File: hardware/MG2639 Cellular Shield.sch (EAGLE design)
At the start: 50 parts, among them J1 SIMHOLDER, Q1 MMBT2222A, Q2 MMBT2222A, U1 TXB0108, U2 SPX29302, U4 ARDUINO_R3_SHIELDNOLABELS, U5 MG2639V3

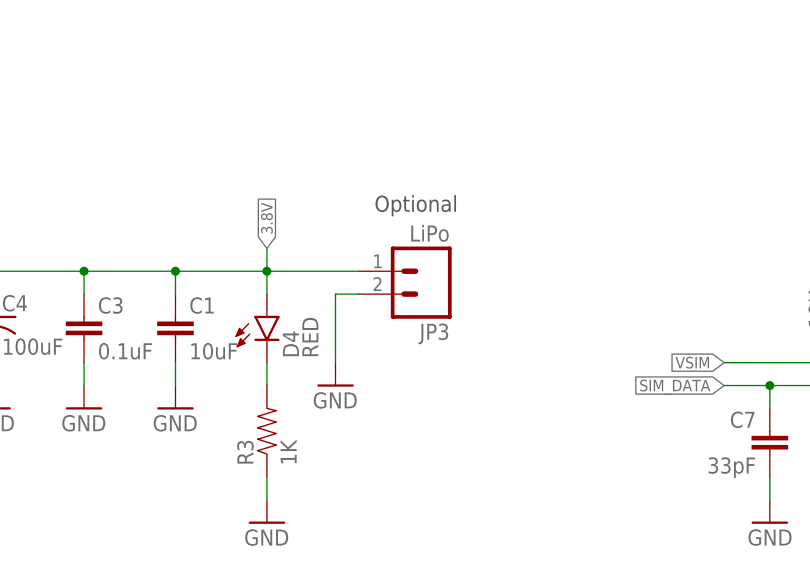
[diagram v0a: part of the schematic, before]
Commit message: Corrected +/- on battery connector
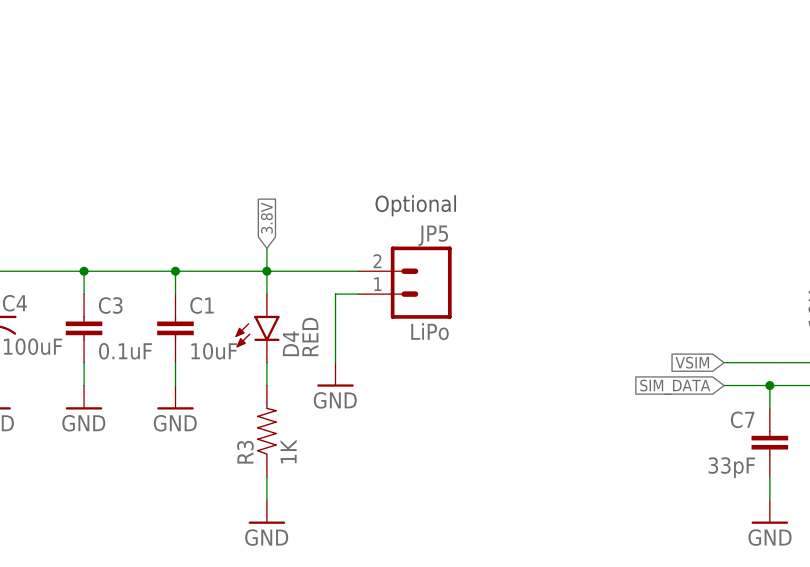
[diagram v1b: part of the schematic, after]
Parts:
- removed JP3: LiPo, SparkFun-Connectors:M02JST-PTH-2
- added JP5: LiPo, SparkFun-Connectors:M02JST-PTH-2
- C10, C11, C3: device SparkFun:CAP0603-CAP -> SparkFun-Capacitors:0.1UF-25V(+80/-20%)(0603)
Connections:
- net 3.8V: now also JP5.2; no longer JP3.1
- net GND: now also JP5.1; no longer JP3.2

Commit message: Prelim firmware. Works for certain features.
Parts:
- BAT1: value 20mm coincell -> 12mm coincell
- D2: value RED -> BLUE; device SparkFun-LED:LED-RED1206 -> SparkFun-LED:LED-BLUE1206
- U4: value ARDUINO_R3_SHIELDNOLABELS -> ARDUINO_R3_SHIELD
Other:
- note added: "N. Seidle"
- note added: "Open SJ1 to disconnect GPS power from board power."
- note added: "Open SJ2 to free up GPIO and power up via boot button."
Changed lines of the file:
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@@
 <part name="GND12" library="SparkFun" deviceset="GND" device=""/>
 <part name="C4" library="SparkFun-Capacitors" deviceset="100UF-10V-10%(TANT)" device="" value="100uF"/>
-<part name="U4" library="SparkFun-Boards" deviceset="ARDUINO_R3_SHIELD" device="NOLABELS" value="ARDUINO_R3_SHIELDNOLABELS"/>
+<part name="U4" library="SparkFun-Boards" deviceset="ARDUINO_R3_SHIELD" device="NOLABELS" value="ARDUINO_R3_SHIELD"/>
 <part name="Q1" library="SparkFun-DiscreteSemi" deviceset="TRANSISTOR_NPN" device="MMBT2222A" value="MMBT2222A"/>
 <part name="Q2" library="SparkFun-DiscreteSemi" deviceset="TRANSISTOR_NPN" device="MMBT2222A" value="MMBT2222A"/>
@@
 <part name="GND13" library="SparkFun" deviceset="GND" device=""/>
 <part name="SJ1" library="SparkFun-Passives" deviceset="JUMPER-PAD-2-NC_BY_TRACE" device="" value=""/>
-<part name="BAT1" library="SparkFun-Electromechanical" deviceset="BATTERY" device="12MM" value="20mm coincell"/>
+<part name="BAT1" library="SparkFun-Electromechanical" deviceset="BATTERY" device="12MM" value="12mm coincell"/>
 <part name="GND15" library="SparkFun" deviceset="GND" device=""/>
 <part name="GND16" library="SparkFun" deviceset="GND" device=""/>
@@
 <part name="R8" library="SparkFun-Resistors" deviceset="1KOHM1/10W1%(0603)" device="" value="1K"/>
 <part name="GND18" library="SparkFun" deviceset="GND" device=""/>
-<part name="D2" library="SparkFun-LED" deviceset="LED-RED" device="1206" value="RED"/>
+<part name="D2" library="SparkFun-LED" deviceset="LED-BLUE" device="1206" value="BLUE"/>
 <part name="R9" library="SparkFun-Resistors" deviceset="1KOHM1/10W1%(0603)" device="" value="1K"/>
 <part name="GND19" library="SparkFun" deviceset="GND" device=""/>
@@
 for antenna U.FL
 wire relief</text>
+<text x="20.32" y="2.54" size="1.778" layer="97">N. Seidle</text>
+<text x="7.62" y="170.18" size="1.778" layer="97">Open SJ1 to disconnect GPS
+power from board power.</text>
+<text x="88.9" y="149.86" size="1.778" layer="97">Open SJ2 to free up GPIO
+and power up via boot button.</text>
 </plain>
 <instances>
@@
 <attribute name="VALUE" x="22.86" y="152.4" size="1.778" layer="96"/>
 </instance>
-<instance part="BAT1" gate="G$1" x="109.22" y="109.22" rot="R270"/>
+<instance part="BAT1" gate="G$1" x="109.22" y="109.22" smashed="yes" rot="R270">
+<attribute name="NAME" x="116.332" y="105.41" size="1.778" layer="95" rot="R90"/>
+<attribute name="VALUE" x="103.632" y="100.076" size="1.778" layer="96" rot="R90"/>
+</instance>
 <instance part="GND15" gate="1" x="109.22" y="99.06" rot="MR0"/>
 <instance part="GND16" gate="1" x="30.48" y="38.1" rot="MR0"/>

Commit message: Add silk labels to pins/jumpers. Add FTDI header. Remove SYSRST circuit. Reconfiguring jumpers. Removed USB connector, broke USB pins out to headers.
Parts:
- removed LOGO1: SFE_LOGO_NAME_FLAME.1_INCH, SparkFun-Aesthetics:SFE_LOGO_NAME_FLAME.1_INCH
- removed Q2: MMBT2222A, SparkFun-DiscreteSemi:TRANSISTOR_NPNMMBT2222A
- removed R11, R12: 22, SparkFun-Resistors:22OHM1/10W1%(0603)
- removed R13: 4.7K, SparkFun-Resistors:4.7KOHM1/10W1%(0603)
- removed U$1: CREATIVE_COMMONS, SparkFun:CREATIVE_COMMONS
- removed U$2: SMA_HOLE, SparkFun-RF:SMA_HOLE
- added FRAME1: FRAME-LEDGER, SparkFun-Aesthetics:FRAME-LEDGER
- added JP3: M01PTH, SparkFun-Connectors:M01PTH
- added JP6: FTDI_BASICPTH, SparkFun-Connectors:FTDI_BASICPTH
- added LOGO4: SFE_LOGO_NAME.1_INCH, SparkFun-Aesthetics:SFE_LOGO_NAME.1_INCH
- added R5: 1K, SparkFun-Resistors:1KOHM1/10W1%(0603)
- JP1: value USBSMD -> (none); device SparkFun-Connectors:USBSMD -> SparkFun-Connectors:M05PTH
- JP2: value (none) -> AUDIO
- S2: value BOOT -> RESET
- SJ2: value JUMPER-PAD-2-NC_BY_TRACE -> JUMPER-PAD-3-2OF3_NC_BY_TRACE; device SparkFun-Passives:JUMPER-PAD-2-NC_BY_TRACE -> SparkFun-Passives:JUMPER-PAD-3-2OF3_NC_BY_TRACE
- SJ3, SJ4, SJ5: value JUMPER-PAD-3-2OF3_NC_BY_PASTE -> JUMPER-PAD-3-2OF3_NC_BY_TRACE; device SparkFun-Passives:JUMPER-PAD-3-2OF3_NC_BY_PASTE -> SparkFun-Passives:JUMPER-PAD-3-2OF3_NC_BY_TRACE
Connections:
- removed net N$10: JP1.D+, R11.1
- removed net N$11: JP1.D-, R12.1
- removed net N$2: Q2.B, R13.2
- new net N$6: R5.1, SJ2.1
- net !SYSRST: now also JP3.1; no longer Q2.C
- net 5V: now also R5.2
- net CELL_RESET: no longer R13.1
- net GND: now also JP1.1, JP6.6; no longer JP1.GND, Q2.E
- net GRX-HV: now also JP6.3
- net GTX-HV: now also JP6.2
- net ON/OFF: now also SJ2.3; no longer SJ2.1
- net RX-SOFT: now also SJ4.3; no longer SJ4.1
- net RXI: now also SJ4.1; no longer SJ4.3
- net TX-SOFT: now also SJ3.3; no longer SJ3.1
- net TXO: now also SJ3.1; no longer SJ3.3
- net USB+: now also JP1.3; no longer R11.2
- net USB-: now also JP1.4; no longer R12.2
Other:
- note added: "Arduino Shield"
- note added: "Boot Button"
- note added: "GPS Battery"
- note added: "Level Shifter"
- note added: "MG2639 Cellular Module"
- note added: "Misc. Headers"
- note added: "Nathan Seidle Jim Lindblom"
- note added: "SIM Card"
- note added: "Select between hardware UART and software UART Default = Software"
- note added: "UART Select"
- note added: "Voltage Regulator"
- note added: "v10"
- note removed: "GRX-2.8V"
- note removed: "GTX"
- note removed: "Holes in board are for antenna U.FL wire relief"
- note removed: "N. Seidle"
- note removed: "Open SJ2 to free up GPIO and power up via boot button."
- note removed: "SMA Bulkhead mount Experimental"
- note removed: "Select between hardware UART and software UART Default = Hardware"
- note removed: "TX-2.8V"
- note removed: "TX-HV"
- note removed: "USB Port Experimental"
- moved on the sheet: BAT1, C1, C10, C11, C2, C3, C4, C5, C6, C7, C8, C9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

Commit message: re-routing around TXB0108, cleaning up some silk.
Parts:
- added FID1, FID2: FIDUCIAL1X2, SparkFun-Aesthetics:FIDUCIAL1X2
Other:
- moved on the sheet: S2

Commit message: adding 22 ohm resistors to D+/D-. placing more vias around vreg.
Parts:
- added R11, R7: 22, SparkFun-Resistors:22OHM1/10W1%(0603)
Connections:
- new net N$10: JP1.3, R11.1
- new net N$2: JP1.4, R7.1
- net USB+: now also R11.2; no longer JP1.3
- net USB-: now also R7.2; no longer JP1.4
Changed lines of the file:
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@@
 <part name="SUPPLY4" library="SparkFun-Aesthetics" deviceset="5V" device=""/>
 <part name="SUPPLY5" library="SparkFun-Aesthetics" deviceset="3.3V" device=""/>
+<part name="R7" library="SparkFun-Resistors" deviceset="22OHM1/10W1%(0603)" device="" value="22"/>
+<part name="R11" library="SparkFun-Resistors" deviceset="22OHM1/10W1%(0603)" device="" value="22"/>
 </parts>
 <sheets>
@@
 <instance part="SUPPLY4" gate="G$1" x="388.62" y="233.68"/>
 <instance part="SUPPLY5" gate="G$1" x="393.7" y="233.68"/>
+<instance part="R7" gate="G$1" x="358.14" y="119.38" smashed="yes">
+<attribute name="NAME" x="359.8164" y="120.5992" size="1.778" layer="95"/>
+<attribute name="VALUE" x="354.7364" y="120.5992" size="1.778" layer="96"/>
+</instance>
+<instance part="R11" gate="G$1" x="358.14" y="116.84" smashed="yes">
+<attribute name="NAME" x="358.902" y="113.7666" size="1.778" layer="95"/>
+<attribute name="VALUE" x="353.822" y="113.7666" size="1.778" layer="96"/>
+</instance>
 </instances>
 <busses>
@@
 <net name="USB+" class="0">
 <segment>
-<label x="355.6" y="116.84" size="1.27" layer="95" xref="yes"/>
-<wire x1="347.98" y1="116.84" x2="355.6" y2="116.84" width="0.1524" layer="91"/>
-<pinref part="JP1" gate="G$1" pin="3"/>
-</segment>
-<segment>
 <pinref part="U5" gate="U1" pin="USB_DP"/>
 <wire x1="241.3" y1="68.58" x2="243.84" y2="68.58" width="0.1524" layer="91"/>
 <label x="243.84" y="68.58" size="1.27" layer="95" xref="yes"/>
 </segment>
+<segment>
+<pinref part="R11" gate="G$1" pin="2"/>
+<wire x1="363.22" y1="116.84" x2="365.76" y2="116.84" width="0.1524" layer="91"/>
+<label x="365.76" y="116.84" size="1.27" layer="95" xref="yes"/>
+</segment>
 </net>
 <net name="USB-" class="0">
-<segment>
-<label x="355.6" y="119.38" size="1.27" layer="95" xref="yes"/>
-<wire x1="347.98" y1="119.38" x2="355.6" y2="119.38" width="0.1524" layer="91"/>
-<pinref part="JP1" gate="G$1" pin="4"/>
-</segment>
 <segment>
 <pinref part="U5" gate="U1" pin="USB_DM"/>
 <wire x1="241.3" y1="66.04" x2="243.84" y2="66.04" width="0.1524" layer="91"/>
 <label x="243.84" y="66.04" size="1.27" layer="95" xref="yes"/>
+</segment>
+<segment>
+<pinref part="R7" gate="G$1" pin="2"/>
+<wire x1="363.22" y1="119.38" x2="365.76" y2="119.38" width="0.1524" layer="91"/>
+<label x="365.76" y="119.38" size="1.27" layer="95" xref="yes"/>
 </segment>
 </net>
@@
 </segment>
 </net>
+<net name="N$2" class="0">
+<segment>
+<pinref part="R7" gate="G$1" pin="1"/>
+<pinref part="JP1" gate="G$1" pin="4"/>
+<wire x1="353.06" y1="119.38" x2="347.98" y2="119.38" width="0.1524" layer="91"/>
+</segment>
+</net>
+<net name="N$10" class="0">
+<segment>
+<pinref part="R11" gate="G$1" pin="1"/>
+<pinref part="JP1" gate="G$1" pin="3"/>
+<wire x1="353.06" y1="116.84" x2="347.98" y2="116.84" width="0.1524" layer="91"/>
+</segment>
+</net>

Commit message: rearranging LEDs - moving GPS LED up with others.
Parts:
- added JP7: M01PTH, SparkFun-Connectors:M01PTH
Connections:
- new net ADCIN: U5.ADCIN
- new net GPIO0: U5.GPIO0/PWM
- new net GPIO1: U5.GPIO1/SCL
- new net GPIO2: U5.GPIO2/SDA
- net VDDIO: now also JP7.1
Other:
- moved on the sheet: JP2
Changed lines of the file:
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@@
 <part name="R7" library="SparkFun-Resistors" deviceset="22OHM1/10W1%(0603)" device="" value="22"/>
 <part name="R11" library="SparkFun-Resistors" deviceset="22OHM1/10W1%(0603)" device="" value="22"/>
+<part name="JP7" library="SparkFun-Connectors" deviceset="M01" device="PTH" value="M01PTH"/>
 </parts>
 <sheets>
@@
 <instance part="JP4" gate="G$1" x="340.36" y="144.78" rot="MR180"/>
 <instance part="GND27" gate="1" x="350.52" y="137.16"/>
-<instance part="JP2" gate="G$1" x="259.08" y="55.88" rot="R180"/>
-<instance part="GND3" gate="1" x="251.46" y="40.64" rot="MR0"/>
+<instance part="JP2" gate="G$1" x="264.16" y="55.88" rot="R180"/>
+<instance part="GND3" gate="1" x="256.54" y="40.64" rot="MR0"/>
 <instance part="C10" gate="G$1" x="210.82" y="251.46"/>
 <instance part="C11" gate="G$1" x="223.52" y="251.46"/>
@@
 <attribute name="VALUE" x="353.822" y="113.7666" size="1.778" layer="96"/>
 </instance>
+<instance part="JP7" gate="G$1" x="337.82" y="165.1"/>
 </instances>
 <busses>
@@
 <segment>
 <pinref part="JP2" gate="G$1" pin="7"/>
-<wire x1="254" y1="45.72" x2="251.46" y2="45.72" width="0.1524" layer="91"/>
-<wire x1="251.46" y1="45.72" x2="251.46" y2="43.18" width="0.1524" layer="91"/>
+<wire x1="259.08" y1="45.72" x2="256.54" y2="45.72" width="0.1524" layer="91"/>
+<wire x1="256.54" y1="45.72" x2="256.54" y2="43.18" width="0.1524" layer="91"/>
 <pinref part="GND3" gate="1" pin="GND"/>
 </segment>
@@
 <label x="210.82" y="259.08" size="1.27" layer="95" rot="R90" xref="yes"/>
 </segment>
+<segment>
+<pinref part="JP7" gate="G$1" pin="1"/>
+<wire x1="345.44" y1="165.1" x2="347.98" y2="165.1" width="0.1524" layer="91"/>
+<label x="347.98" y="165.1" size="1.27" layer="95" xref="yes"/>
+</segment>
 </net>
 <net name="USB+" class="0">
@@
 <segment>
 <pinref part="U5" gate="U1" pin="MIC_P1"/>
-<wire x1="241.3" y1="55.88" x2="254" y2="55.88" width="0.1524" layer="91"/>
+<wire x1="241.3" y1="55.88" x2="259.08" y2="55.88" width="0.1524" layer="91"/>
 <pinref part="JP2" gate="G$1" pin="3"/>
 </segment>
@@
 <segment>
 <pinref part="U5" gate="U1" pin="MIC_P0"/>
-<wire x1="241.3" y1="58.42" x2="254" y2="58.42" width="0.1524" layer="91"/>
+<wire x1="241.3" y1="58.42" x2="259.08" y2="58.42" width="0.1524" layer="91"/>
 <pinref part="JP2" gate="G$1" pin="2"/>
 </segment>
@@
 <segment>
 <pinref part="U5" gate="U1" pin="MIC_N0"/>
-<wire x1="241.3" y1="60.96" x2="254" y2="60.96" width="0.1524" layer="91"/>
+<wire x1="241.3" y1="60.96" x2="259.08" y2="60.96" width="0.1524" layer="91"/>
 <pinref part="JP2" gate="G$1" pin="1"/>
 </segment>
@@
 <segment>
 <pinref part="U5" gate="U1" pin="RECN"/>
-<wire x1="241.3" y1="53.34" x2="254" y2="53.34" width="0.1524" layer="91"/>
+<wire x1="241.3" y1="53.34" x2="259.08" y2="53.34" width="0.1524" layer="91"/>
 <pinref part="JP2" gate="G$1" pin="4"/>
 </segment>
@@
 <segment>
 <pinref part="U5" gate="U1" pin="RECP"/>
-<wire x1="241.3" y1="50.8" x2="254" y2="50.8" width="0.1524" layer="91"/>
+<wire x1="241.3" y1="50.8" x2="259.08" y2="50.8" width="0.1524" layer="91"/>
 <pinref part="JP2" gate="G$1" pin="5"/>
 </segment>
@@
 <segment>
 <pinref part="U5" gate="U1" pin="EAR_L"/>
-<wire x1="241.3" y1="48.26" x2="254" y2="48.26" width="0.1524" layer="91"/>
+<wire x1="241.3" y1="48.26" x2="259.08" y2="48.26" width="0.1524" layer="91"/>
 <pinref part="JP2" gate="G$1" pin="6"/>
 </segment>
@@
 </segment>
 </net>
+<net name="GPIO0" class="0">
+<segment>
+<pinref part="U5" gate="U1" pin="GPIO0/PWM"/>
+<wire x1="241.3" y1="106.68" x2="243.84" y2="106.68" width="0.1524" layer="91"/>
+<label x="243.84" y="106.68" size="1.27" layer="95" xref="yes"/>
+</segment>
+</net>
+<net name="GPIO1" class="0">
+<segment>
+<pinref part="U5" gate="U1" pin="GPIO1/SCL"/>
+<wire x1="241.3" y1="104.14" x2="243.84" y2="104.14" width="0.1524" layer="91"/>
+<label x="243.84" y="104.14" size="1.27" layer="95" xref="yes"/>
+</segment>
+</net>
+<net name="GPIO2" class="0">
+<segment>
+<pinref part="U5" gate="U1" pin="GPIO2/SDA"/>
+<wire x1="241.3" y1="101.6" x2="243.84" y2="101.6" width="0.1524" layer="91"/>
+<label x="243.84" y="101.6" size="1.27" layer="95" xref="yes"/>
+</segment>
+</net>
+<net name="ADCIN" class="0">
+<segment>
+<pinref part="U5" gate="U1" pin="ADCIN"/>
+<wire x1="241.3" y1="43.18" x2="243.84" y2="43.18" width="0.1524" layer="91"/>
+<label x="243.84" y="43.18" size="1.27" layer="95" xref="yes"/>
+</segment>
+</net>

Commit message: Switching TXB0108 to a TXB0104. Breaking out I2C pins, 2.8V. Fixing some silk.
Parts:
- removed JP7: M01PTH, SparkFun-Connectors:M01PTH
- C2: value 10uF -> 33pF; device SparkFun-Capacitors:10UF50V20%(1210) -> SparkFun-Capacitors:33PF-50V-5%-(0603)
- C3: value 0.1uF -> 33pF; device SparkFun-Capacitors:0.1UF-25V(+80/-20%)(0603) -> SparkFun-Capacitors:33PF-50V-5%-(0603)
- C4: value 100uF -> 1.0uF; device SparkFun-Capacitors:100UF-10V-10%(TANT) -> SparkFun-Capacitors:1.0UF-16V-10%(0603)
- C6: value 1.0uF -> 100uF; device SparkFun-Capacitors:1.0UF-16V-10%(0603) -> SparkFun-Capacitors:100UF-10V-10%(TANT)
- C8: value 33pF -> 0.1uF; device SparkFun-Capacitors:33PF-50V-5%-(0603) -> SparkFun-Capacitors:0.1UF-25V(+80/-20%)(0603)
- C9: value 33pF -> 10uF; device SparkFun-Capacitors:33PF-50V-5%-(0603) -> SparkFun-Capacitors:10UF50V20%(1210)
- JP1: value (none) -> LiPo; device SparkFun-Connectors:M05PTH -> SparkFun-Connectors:M02JST-PTH-2
- JP3: value M01PTH -> FTDI_BASICPTH; device SparkFun-Connectors:M01PTH -> SparkFun-Connectors:FTDI_BASICPTH
- JP4: device SparkFun-Connectors:M03PTH -> SparkFun-Connectors:M07
- JP5: value LiPo -> (none); device SparkFun-Connectors:M02JST-PTH-2 -> SparkFun-Connectors:M05PTH
- JP6: value FTDI_BASICPTH -> M02PTH; device SparkFun-Connectors:FTDI_BASICPTH -> SparkFun-Connectors:M02PTH
- LOGO2: value OSHW-LOGOS -> SFE_LOGO_NAME_FLAME.2_INCH; device SparkFun-Aesthetics:OSHW-LOGOS -> SparkFun-Aesthetics:SFE_LOGO_NAME_FLAME.2_INCH
- LOGO3: value SFE_LOGO_NAME_FLAME.2_INCH -> OSHW-LOGOS; device SparkFun-Aesthetics:SFE_LOGO_NAME_FLAME.2_INCH -> SparkFun-Aesthetics:OSHW-LOGOS
- R1: value 1K -> 10K; device SparkFun-Resistors:1KOHM1/10W1%(0603) -> SparkFun-Resistors:10KOHM1/10W1%(0603)0603
- R10: value 10K -> 22; device SparkFun-Resistors:10KOHM1/10W1%(0603)0603 -> SparkFun-Resistors:22OHM1/10W1%(0603)
- R2: value 4.7K -> 1K; device SparkFun-Resistors:4.7KOHM1/10W1%(0603) -> SparkFun-Resistors:1KOHM1/10W1%(0603)
- R3: value 1K -> 4.7K; device SparkFun-Resistors:1KOHM1/10W1%(0603) -> SparkFun-Resistors:4.7KOHM1/10W1%(0603)
- R7: value 22 -> 1K; device SparkFun-Resistors:22OHM1/10W1%(0603) -> SparkFun-Resistors:1KOHM1/10W1%(0603)
- SJ1, SJ6: value JUMPER-PAD-2-NC_BY_TRACE -> JUMPER-PAD-3-2OF3_NC_BY_TRACE; device SparkFun-Passives:JUMPER-PAD-2-NC_BY_TRACE -> SparkFun-Passives:JUMPER-PAD-3-2OF3_NC_BY_TRACE
- SJ2, SJ3: value JUMPER-PAD-3-2OF3_NC_BY_TRACE -> JUMPER-PAD-2-NC_BY_TRACE; device SparkFun-Passives:JUMPER-PAD-3-2OF3_NC_BY_TRACE -> SparkFun-Passives:JUMPER-PAD-2-NC_BY_TRACE
- U1: value TXB0108 -> SPX29302; device Testing:TXB0108 -> SparkFun-PowerIC:SPX29302
- U2: value SPX29302 -> (none); device SparkFun-PowerIC:SPX29302 -> SparkFun-DigitalIC:TXB0104PWRSOIC14
- renumbered D4 to D1, LOGO4 to LOGO1, S3 to S1, U4 to J2, U5 to U3
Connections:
- removed net GPIO0: U3.GPIO0/PWM
- removed net GPIO1: U3.GPIO1/SCL
- removed net GPIO2: U3.GPIO2/SDA
- removed net HJ: U1.A3
- removed net JK: U1.A4
- removed net KK: U1.B3
- removed net LL: U1.B4
- removed net RX2-HV: JP4.1, U1.B7
- removed net TX2-HV: JP4.2, U1.B8
- new net GPIO1/SCL: JP4.1, U3.GPIO1/SCL
- new net GPIO2/SDA: JP4.2, U3.GPIO2/SDA
- net !SYSRST: now also JP4.7; no longer JP3.1
- net 3.3V: now also SJ4.3; no longer SJ5.3
- net 3.8V: now also C6.+, C8.1, C9.1, JP1.2, JP6.2, SJ2.2, SJ3.1; no longer C1.1, C3.1, C4.+, JP5.2, SJ1.1, SJ6.2
- net 5V: now also R2.2, SJ4.1; no longer R5.2, SJ5.1
- net ADJUST: now also R5.2, U1.ADJUST; no longer R1.2, U2.ADJUST
- net GND: now also C1.1, C2.2, C4.2, C6.-, JP3.6, JP4.4, JP6.1, R5.1, R7.1, U1.GND@0, U1.GND@1, U2.GND; no longer C1.2, C2.1, C4.-, C6.2, JP4.3, JP6.6, R1.1, R3.1, U1.GND, U2.GND@0, U2.GND@1
- net GRX-2.8V: now also U2.A2; no longer U1.A2
- net GRX-HV: now also JP3.3, U2.B2; no longer JP6.3, U1.B2
- net GTX-2.8V: now also U2.A1; no longer U1.A1
- net GTX-HV: now also JP3.2, U2.B1; no longer JP6.2, U1.B1
- net N$1: now also R1.2, U1.ENABLE; no longer R6.2, U2.ENABLE
- net N$10: now also JP5.3; no longer JP1.3
- net N$17: now also R7.2; no longer R3.2
- net N$2: now also JP5.4, R10.1; no longer JP1.4, R7.1
- net N$3: now also R3.2; no longer R2.2
- net N$4: now also SJ2.1, U1.VOUT; no longer SJ6.1, U2.VOUT
- net N$5: now also R3.1, SJ1.2; no longer R2.1, SJ2.2
- net N$6: now also R2.1, SJ1.1; no longer R5.1, SJ2.1
- net N$8: now also R9.2; no longer R8.2
- net N$9: now also R8.2; no longer R9.2
- net ON/OFF: now also SJ1.3; no longer SJ2.3
- net RX-2.8V: now also U2.A3; no longer U1.A5
- net RX-HV: now also SJ5.2, U2.B3; no longer SJ3.2, U1.B5
- net RX-SOFT: now also SJ6.3; no longer SJ4.3
- net RX2-2.8V: now also JP4.6; no longer U1.A7
- net RXI: now also SJ6.1; no longer SJ4.1
- net SIM_CLK: now also C3.1; no longer C8.1
- net SIM_DATA: now also R6.1; no longer R10.1
- net SIM_RST: now also C2.1; no longer C9.1
- net TX-2.8V: now also U2.A4; no longer U1.A6
- net TX-HV: now also SJ6.2, U2.B4; no longer SJ4.2, U1.B6
- net TX-SOFT: now also SJ5.3; no longer SJ3.3
- net TX2-2.8V: now also JP4.5; no longer U1.A8
- net TXO: now also SJ5.1; no longer SJ3.1
- net USB-: now also R10.2; no longer R7.2
- net VCCB: now also SJ4.2, U2.VCCB; no longer SJ5.2, U1.VCCB
- net VDDIO: now also JP4.3, U2.OE, U2.VCCA; no longer JP7.1, U1.OE, U1.VCCA
- net VRAW: now also C1.2, R1.1, U1.VIN; no longer C2.2, R6.1, U2.VIN
- net VSIM: now also C4.1, R6.2; no longer C6.1, R10.2
- net V_GPS: now also SJ3.2; no longer SJ1.2
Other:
- note added: "FTDI Header to debug UART1"
- note added: "Top-left header breaks out I2C, UART2, VDDIO, GND and the cell module's reset pin."
- note added: "USB Header matches SFE micro & mini-b breakouts"
- note removed: "2nd Debug Port Experimental"
- moved on the sheet: C1, C2, C3, C8, C9, R1, R10, R11, R2, R3, R5, R6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

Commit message: Routing UART1 to FTDI header instead of GPS. Adding TP's. Fixing silk. Routing out GPS battery pull-out area.
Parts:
- added TP1, TP2: TEST-POINT3X5, SparkFun-Passives:TEST-POINT3X5
- SJ1: value JUMPER-PAD-3-2OF3_NC_BY_TRACE -> JUMPER-PAD-2-NC_BY_TRACE; device SparkFun-Passives:JUMPER-PAD-3-2OF3_NC_BY_TRACE -> SparkFun-Passives:JUMPER-PAD-2-NC_BY_TRACE
- SJ3: value JUMPER-PAD-2-NC_BY_TRACE -> JUMPER-PAD-3-2OF3_NC_BY_TRACE; device SparkFun-Passives:JUMPER-PAD-2-NC_BY_TRACE -> SparkFun-Passives:JUMPER-PAD-3-2OF3_NC_BY_TRACE
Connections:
- net 3.8V: now also SJ1.1; no longer SJ3.1
- net GPS_FIX: now also TP1.1
- net GPS_RTC: now also TP2.1
- net GRX-HV: no longer JP3.3
- net GTX-HV: no longer JP3.2
- net N$5: now also SJ3.2; no longer SJ1.2
- net N$6: now also SJ3.1; no longer SJ1.1
- net ON/OFF: now also SJ3.3; no longer SJ1.3
- net RX-HV: now also JP3.3
- net TX-HV: now also JP3.2
- net V_GPS: now also SJ1.2; no longer SJ3.2
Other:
- note added: "v11"
- note removed: "v10"
